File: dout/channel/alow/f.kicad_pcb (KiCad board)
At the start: 2 copper layers, 19.1 x 10.8 mm, 7 parts, among them J1 dio_channel_i, Q1 BC817, U1 LTV-357T

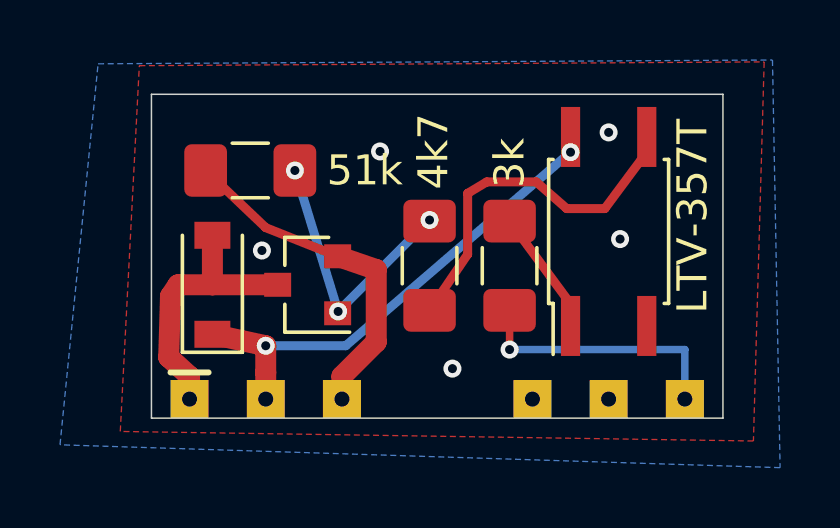
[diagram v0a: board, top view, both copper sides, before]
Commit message: voltage regulator for each module
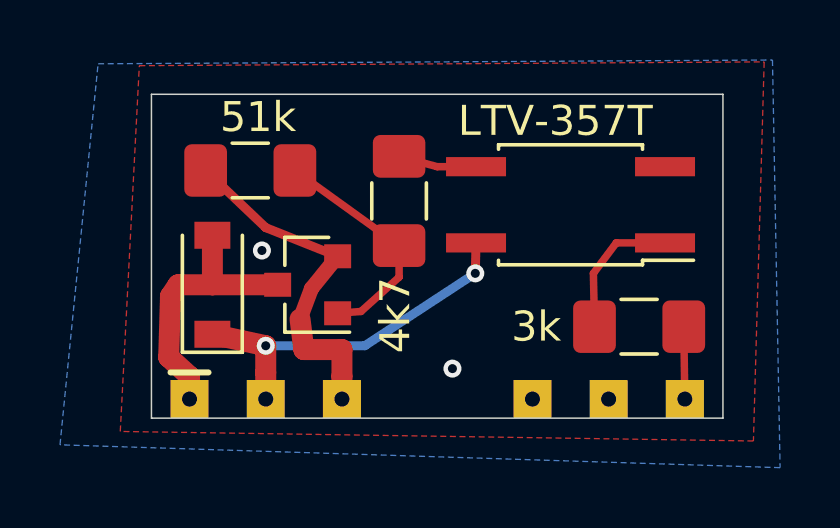
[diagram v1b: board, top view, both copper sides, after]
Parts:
- moved R3 4.77 mm to (177.5, 126.5), turned to 0 degrees
- moved R2 2.39 mm to (169.5, 122.3), turned to 90 degrees
- moved U1 1.55 mm to (175.3, 122.4), turned to 180 degrees
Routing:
- net Net-(R2-Pad2): track 11.6 -> 2.61 mm
- net IN: track 8.67 -> 2.41 mm, vias 1 -> 0
- net VINP: track 16.2 -> 12.3 mm
- net Net-(Q1-Pad1): track 9.23 -> 7.82 mm, vias 3 -> 0
- net GND: vias 5 -> 2
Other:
- board text added: "active low out"
- board text removed: "active low"
